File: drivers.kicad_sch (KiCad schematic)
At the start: 21 parts

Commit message: add truck drivers
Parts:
- removed J? (x4): TE_Faston_20-16AWG_Straight_Tab, TE_Faston_20-16AWG_Straight_Tab, symbol Toadly:TE_Faston_20-16AWG_Straight_Tab
- added J? (x4): TE_Faston_20-16AWG_Straight_Tab, TE_Faston_20-16AWG_Straight_Tab, symbol Toadly:TE_Faston_20-16AWG_Straight_Tab
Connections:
- net FLOOD_D_A: no longer names the net of J?.1 (P1), J?.2 (P1), U?.10 (OUT), U?.11 (OUT)
- net FLOOD_D_B: no longer names the net of J?.1 (P1), J?.2 (P1), U?.8 (OUT), U?.9 (OUT)
- net FLOOD_P_A: no longer names the net of U?.10 (OUT), U?.11 (OUT)
- net FLOOD_P_A: now also J?.1 (P1), J?.2 (P1)
- net FLOOD_P_B: no longer names the net of U?.8 (OUT), U?.9 (OUT)
- net FLOOD_P_B: now also J?.1 (P1), J?.2 (P1)
- net FLOOD_R_A: no longer names the net of U?.10 (OUT), U?.11 (OUT)
- net FLOOD_R_A: now also J?.1 (P1), J?.2 (P1)
- net FLOOD_R_B: no longer names the net of U?.8 (OUT), U?.9 (OUT)
- net FLOOD_R_B: now also J?.1 (P1), J?.2 (P1)
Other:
- moved on the sheet: J?

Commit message: annotate schematic
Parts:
- C7, C8, C9: renamed from C?; footprint (none) -> Capacitor_SMD:C_0805_2012Metric_Pad1.18x1.45mm_HandSolder
- R3, R4, R5: renamed from R?; footprint (none) -> Resistor_SMD:R_0805_2012Metric_Pad1.20x1.40mm_HandSolder
- gave numbers to parts that had none: 9

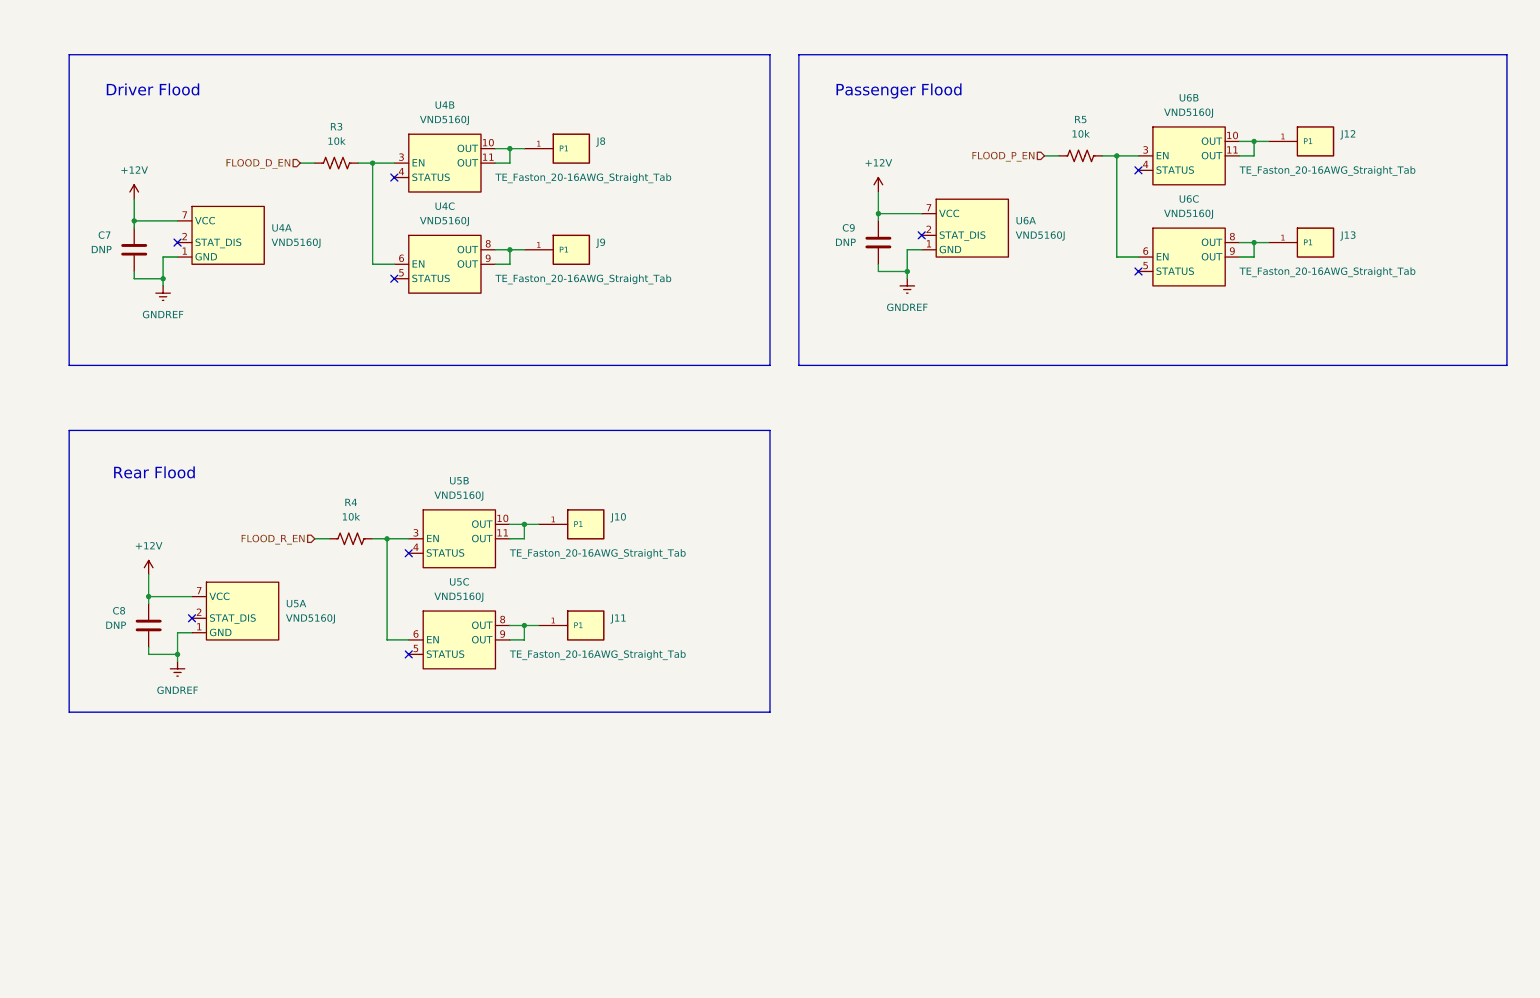
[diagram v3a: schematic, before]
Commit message: add pulldowns for flood light driver control lines
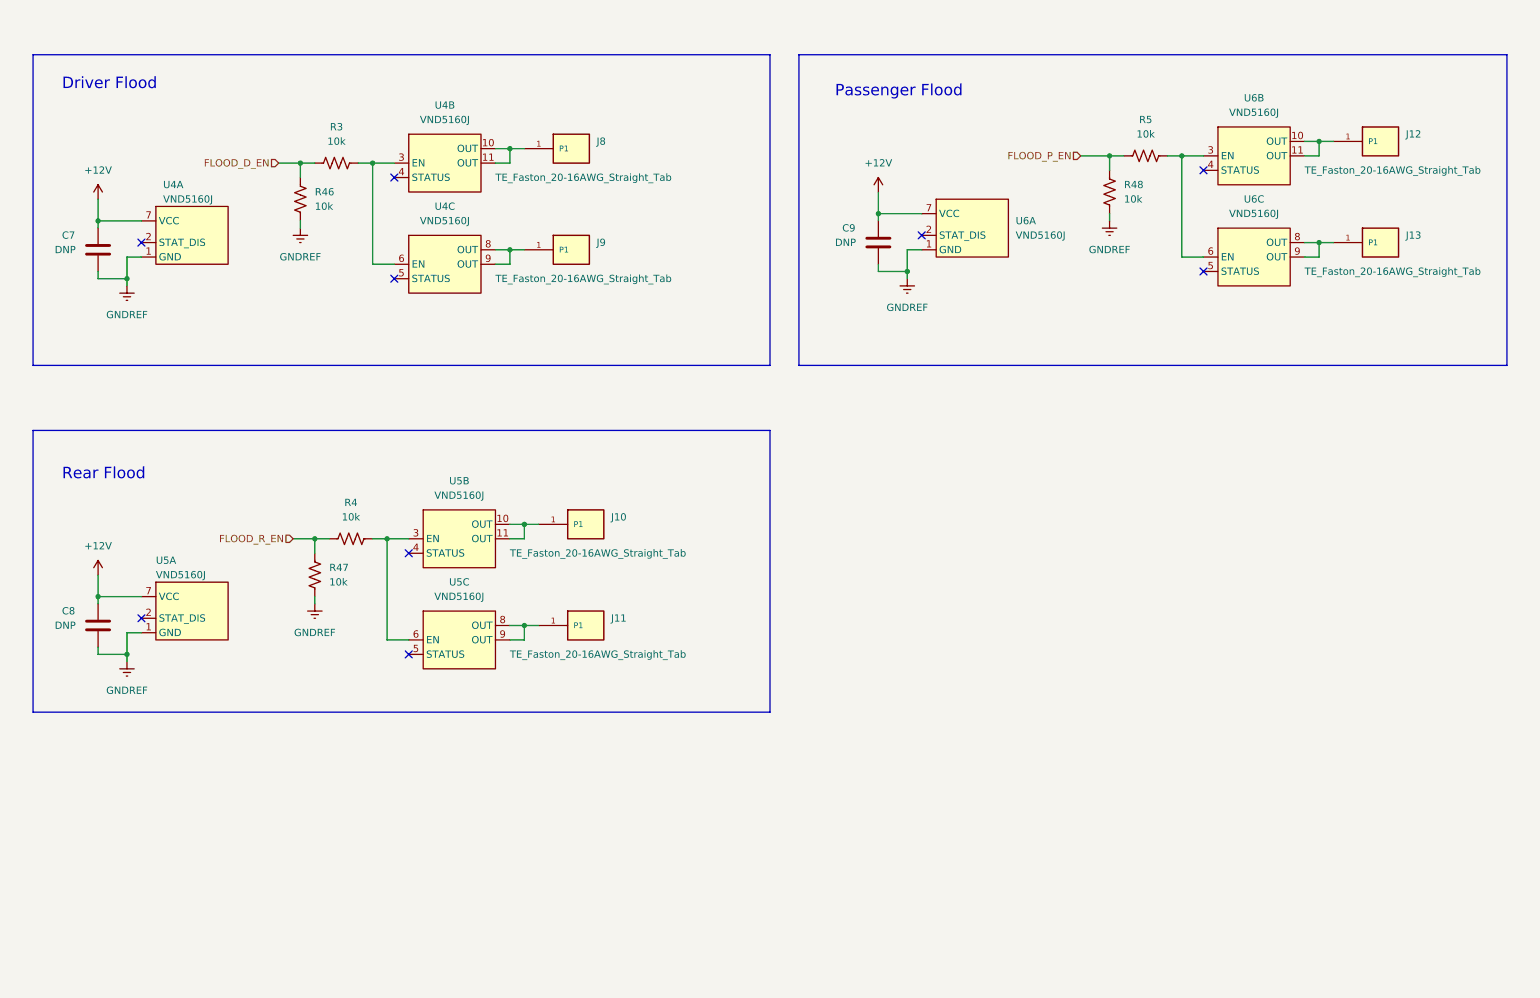
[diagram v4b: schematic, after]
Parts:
- added R46, R47, R48: 10k, Resistor_SMD:R_0805_2012Metric_Pad1.20x1.40mm_HandSolder, symbol Device:R_US
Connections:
- net FLOOD_D_EN: now also R46.2
- net FLOOD_P_EN: now also R48.2
- net FLOOD_R_EN: now also R47.2
- net GNDREF: now also R46.1, R47.1, R48.1
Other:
- moved on the sheet: C7, C8, J12, J13, R5, U4A, U5A, U6B, U6C

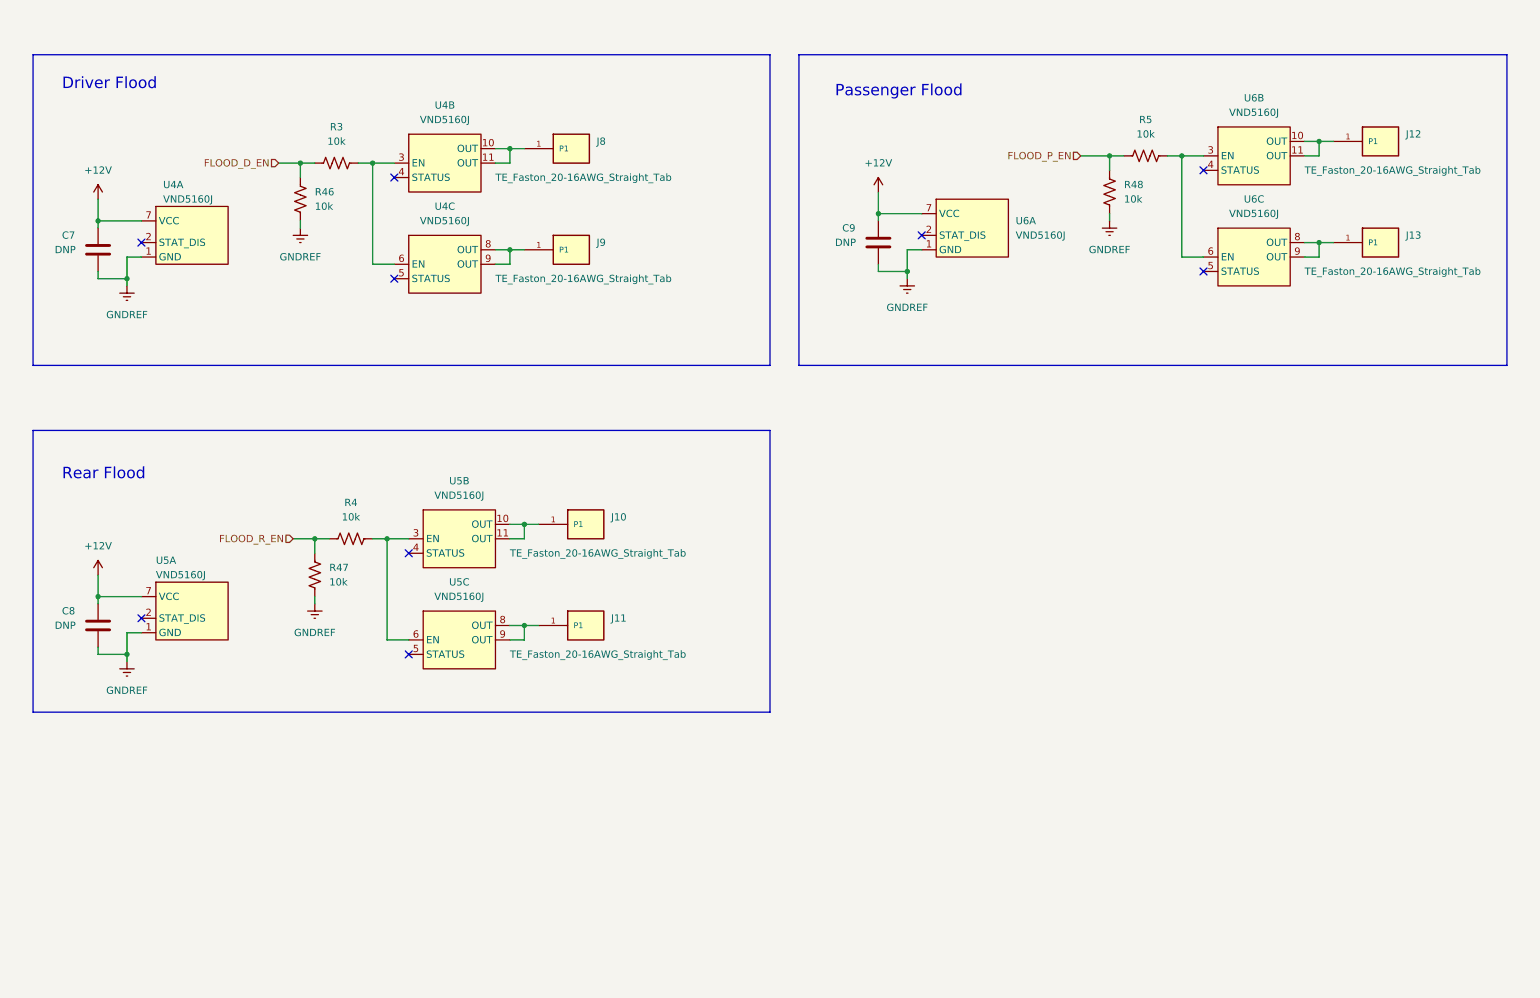
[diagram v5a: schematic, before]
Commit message: add compartment lights, switch to samd21j
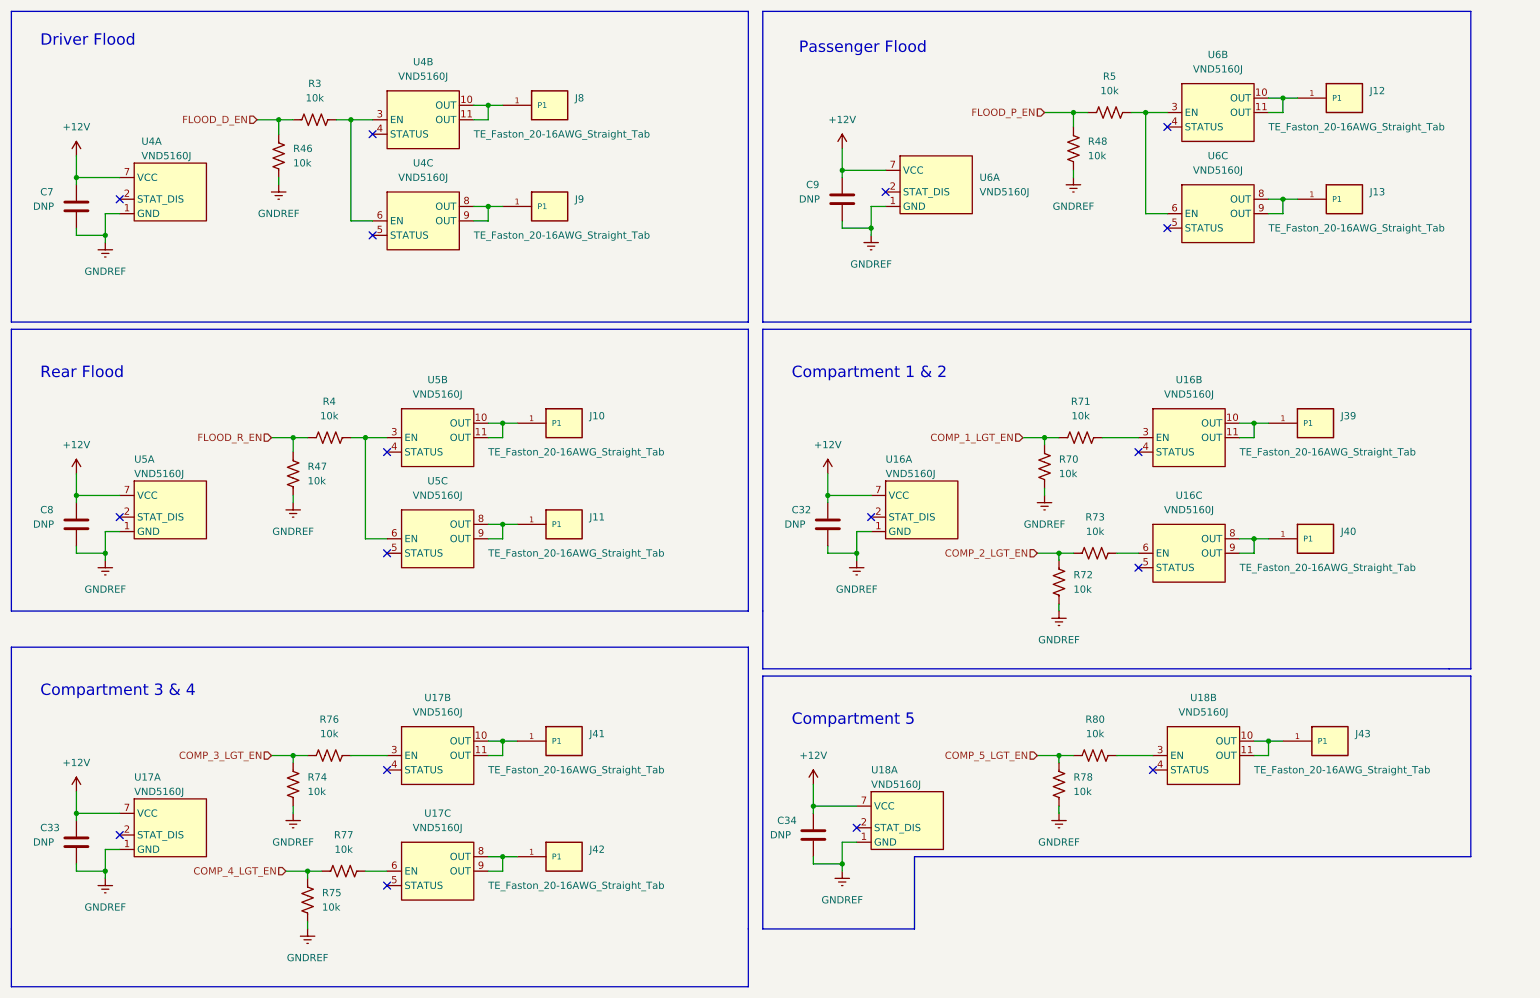
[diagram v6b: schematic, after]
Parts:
- added C32, C33, C34: DNP, Capacitor_SMD:C_0805_2012Metric_Pad1.18x1.45mm_HandSolder, symbol Device:C
- added J39, J40, J41, J42, J43: TE_Faston_20-16AWG_Straight_Tab, TE_Faston_20-16AWG_Straight_Tab, symbol Toadly:TE_Faston_20-16AWG_Straight_Tab
- added R70, R71, R72, R73, R74, R75, R76, R77, R78, R80: 10k, Resistor_SMD:R_0805_2012Metric_Pad1.20x1.40mm_HandSolder, symbol Device:R_US
- added U16, U17, U18: VND5160J, Toadly:POWERSSO-12, symbol Toadly:VND5160J
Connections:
- net +12V: now also C32.1, C33.1, C34.1, U16.12 (VCC), U16.7 (VCC), U16.PAD (VCC), U17.12 (VCC), U17.7 (VCC), U17.PAD (VCC), U18.12 (VCC), U18.7 (VCC), U18.PAD (VCC)
- net GNDREF: now also C32.2, C33.2, C34.2, R70.1, R72.1, R74.1, R75.1, R78.1, U16.1 (GND), U17.1 (GND), U18.1 (GND)
- new net: R71.2, U16.3 (EN)
- new net: R73.2, U16.6 (EN)
- new net: J40.1 (P1), J40.2 (P1), U16.8 (OUT), U16.9 (OUT)
- new net: R80.2, U18.3 (EN)
- new net: J41.1 (P1), J41.2 (P1), U17.10 (OUT), U17.11 (OUT)
- new net: J43.1 (P1), J43.2 (P1), U18.10 (OUT), U18.11 (OUT)
- new net: R76.2, U17.3 (EN)
- new net: J39.1 (P1), J39.2 (P1), U16.10 (OUT), U16.11 (OUT)
- new net: R77.2, U17.6 (EN)
- new net: J42.1 (P1), J42.2 (P1), U17.8 (OUT), U17.9 (OUT)
- new net COMP_1_LGT_EN: R70.2, R71.1
- new net COMP_2_LGT_EN: R72.2, R73.1
- new net COMP_3_LGT_EN: R74.2, R76.1
- new net COMP_4_LGT_EN: R75.2, R77.1
- new net COMP_5_LGT_EN: R78.2, R80.1
- no-connect marks 9 -> 17
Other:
- note added: "Compartment 1 & 2"
- note added: "Compartment 3 & 4"
- note added: "Compartment 5"
- moved on the sheet: C7, C8, C9, J10, J11, J12, J13, J8, J9, R3, R4, R46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
